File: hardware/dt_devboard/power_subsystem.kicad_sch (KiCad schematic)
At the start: 2 parts

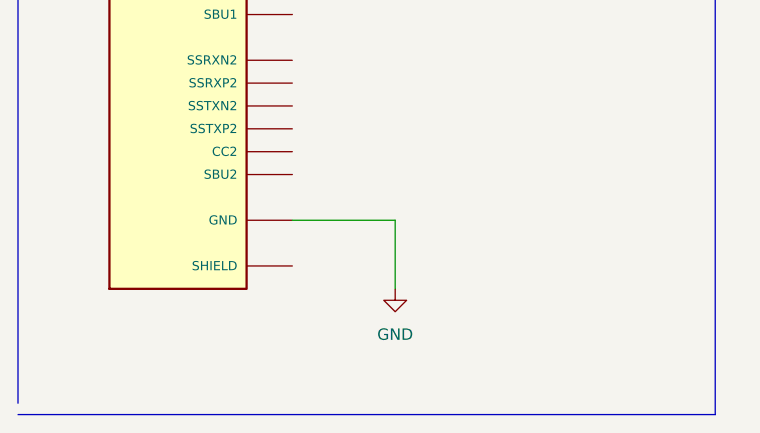
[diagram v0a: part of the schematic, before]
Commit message: added USB signals to MCU
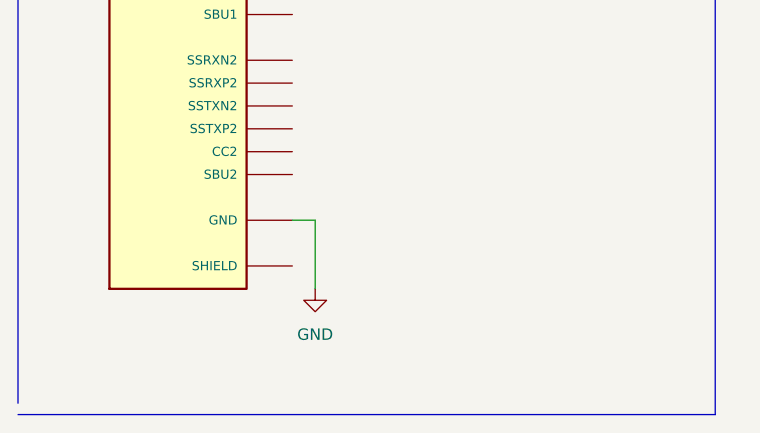
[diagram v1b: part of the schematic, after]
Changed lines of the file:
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@@
     (stroke (width 0) (type default) (color 0 0 0 0))
   )
-  (wire (pts (xy 49.53 91.44) (xy 60.96 91.44))
+  (wire (pts (xy 49.53 91.44) (xy 52.07 91.44))
     (stroke (width 0) (type default) (color 0 0 0 0))
   )
@@
     (stroke (width 0) (type default) (color 0 0 0 0))
   )
-  (wire (pts (xy 60.96 91.44) (xy 60.96 99.06))
+  (wire (pts (xy 52.07 91.44) (xy 52.07 99.06))
     (stroke (width 0) (type default) (color 0 0 0 0))
   )
@@
     (pin "SH6")
   )
-  (symbol (lib_id "power:GND") (at 60.96 99.06 0) (unit 1)
+  (symbol (lib_id "power:GND") (at 52.07 99.06 0) (unit 1)
     (in_bom yes) (on_board yes) (fields_autoplaced)
-    (property "Reference" "#PWR?" (id 0) (at 60.96 105.41 0)
+    (property "Reference" "#PWR?" (id 0) (at 52.07 105.41 0)
       (effects (font (size 1.27 1.27)) hide)
     )
-    (property "Value" "GND" (id 1) (at 60.96 104.14 0))
-    (property "Footprint" "" (id 2) (at 60.96 99.06 0)
+    (property "Value" "GND" (id 1) (at 52.07 104.14 0))
+    (property "Footprint" "" (id 2) (at 52.07 99.06 0)
       (effects (font (size 1.27 1.27)) hide)
     )
-    (property "Datasheet" "" (id 3) (at 60.96 99.06 0)
+    (property "Datasheet" "" (id 3) (at 52.07 99.06 0)
       (effects (font (size 1.27 1.27)) hide)
     )
